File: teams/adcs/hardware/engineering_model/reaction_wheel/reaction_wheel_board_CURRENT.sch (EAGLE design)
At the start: 94 parts, among them U2 TPS732XX, U3 TPS732XX

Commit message: ADCS/RW: Clean up schematic
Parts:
- removed C26, C27: 2.2 μF, rcl:C-USC0805
- removed C32: 1 μF, rcl:C-USC0805
- removed C33: 22 μF, rcl:C-USC1206
- removed C34: 5.6 pF, rcl:C-USC0805
- removed C35: 10 μF, rcl:C-USC0805
- removed C36: 47 μF, rcl:C-USC1206
- removed D5: PMEG6010CEJ, DubSat1 Components:PMEG6010CEJ
- removed L2: WURTH_ELEKTRONIK_INDDD_744877001, DubSat1 Components:WURTH_ELEKTRONIK_INDDD_744877001
- removed R15: 1 kΩ, DubSat1 Components:RESISTOR0805
- removed R16: 330 kΩ, DubSat1 Components:RESISTOR0805
- removed R33: 120 kΩ, DubSat1 Components:RESISTOR0805
- removed U$6: LT8335, DubSat1 Components:LT8335
- C1, C11, C13, C15, C18, C20, C22, C3, C5: device rcl:C-USC1206 -> DubSat1 Components:CAPACITOR0805
- C12, C14, C19, C2, C21, C4: device rcl:C-USC0805 -> DubSat1 Components:CAPACITOR0805
- C16, C29: value 0.01 μF -> 0.01uF
- C17, C28, C30: value 1 μF -> 1uF
- C31: value 1μF -> 1uF
- C8: value 10 uF -> 10uF; device rcl:C-USC0805 -> DubSat1 Components:CAPACITOR0805
- R1, R17, R18, R19, R2, R24, R25, R26, R27, R3, R32, R8: value 3.3K -> 3.3k
- R10, R11, R9: value (none) -> 330
- R20, R21, R22, R28, R29, R30, R4, R5, R6: value 10K -> 10k
- R23, R31, R7: value (none) -> 273k
- U2, U3: value TPS732XX -> LT1761-X; device DubSat1 Components:TPS732XX -> DubSat1 Components:LT1761-X
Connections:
- removed net EN_UVLO: R15.2, U$6.EN/UVLO
- removed net FBX: C34.2, R16.1, R33.2, U$6.FBX
- removed net INT_VCC: C27.1, U$6.INT_VCC
- removed net SW: C32.1, L2.2A, U$6.SW@1, U$6.SW@2
- removed net VD: C32.2, D5.+, L2.1A
- removed net VM: C15.2, C22.2, C33.1, C34.1, C35.1, C36.1, C5.2, D5.-, R16.2, U$12.VM, U$15.VM, U$7.VM
- net GND: no longer C26.2, C27.2, C33.2, C35.2, C36.2, L2.1B, R33.1, U$6.GND
- net VBAT: now also C15.2, C22.2, C5.2, U$12.VM, U$15.VM, U$7.VM; no longer C26.1, L2.2B, R15.1, U$6.V_IN
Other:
- note added: "3v3 LDO"
- note added: "5v LDO"
- note added: "PC104 Header"
- note added: "X Motor Controller"
- note added: "X Motor Driver"
- note added: "Y Motor Controller"
- note added: "Y Motor Driver"
- note added: "Z Motor Controller"
- note added: "Z Motor Driver"
- moved on the sheet: C1, C11, C12, C13, C14, C15, C16, C17, C18, C19, C2, C20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

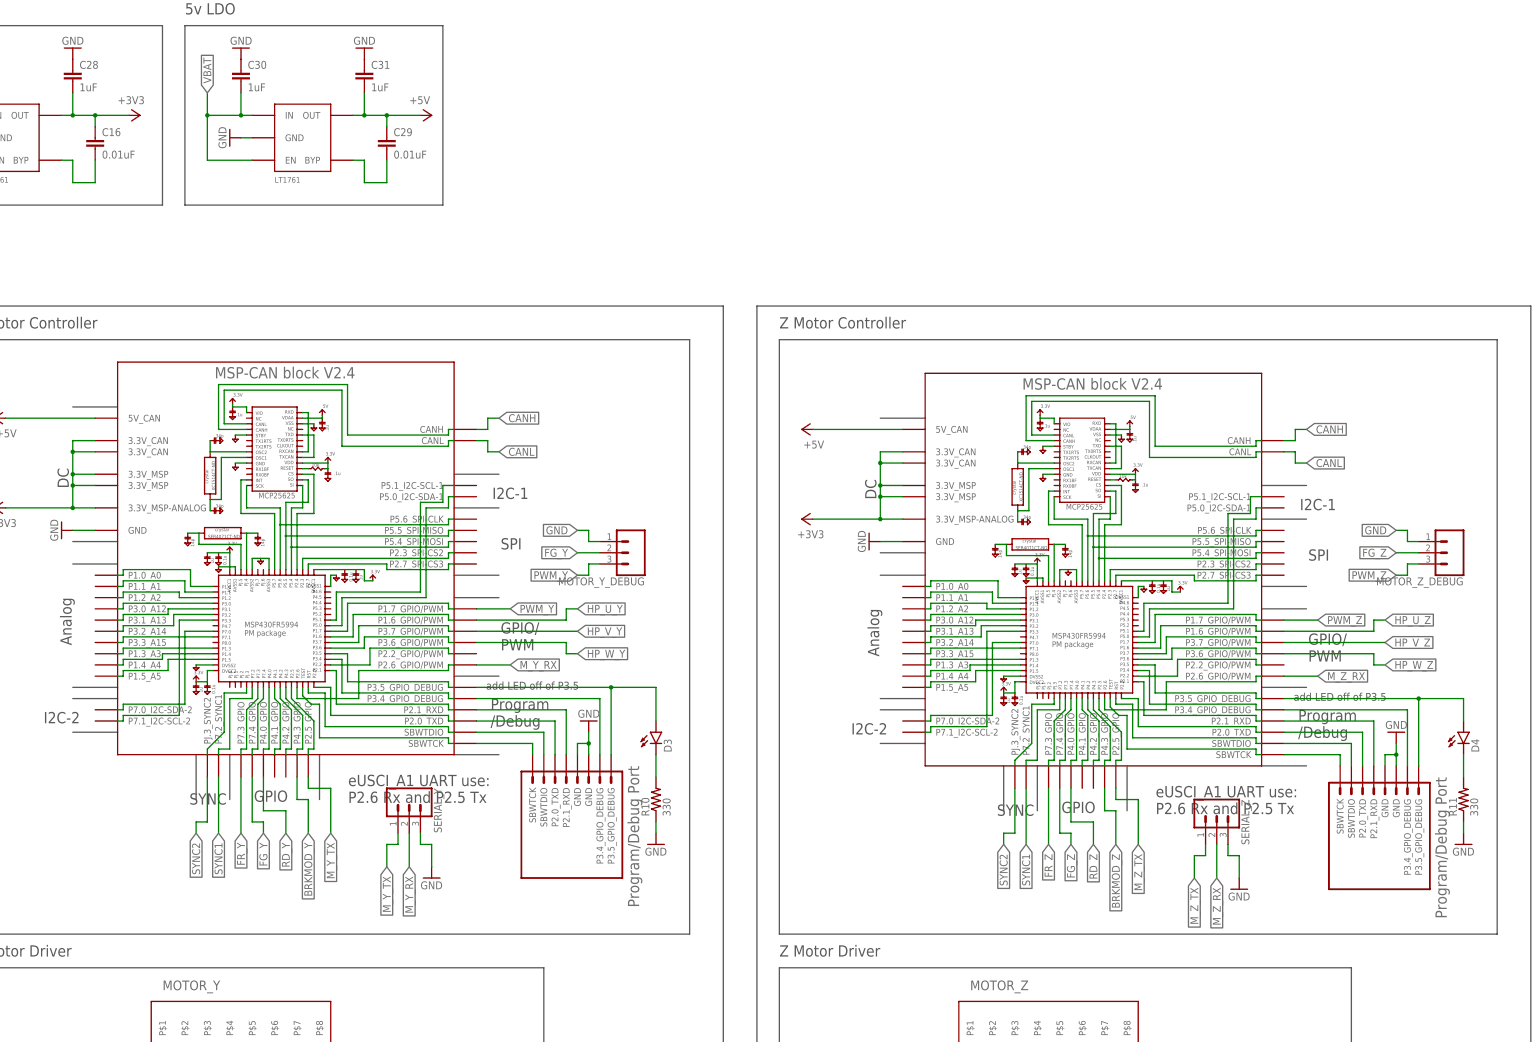
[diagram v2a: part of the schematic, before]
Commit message: ADCS/RW: Update LDO capacitor values
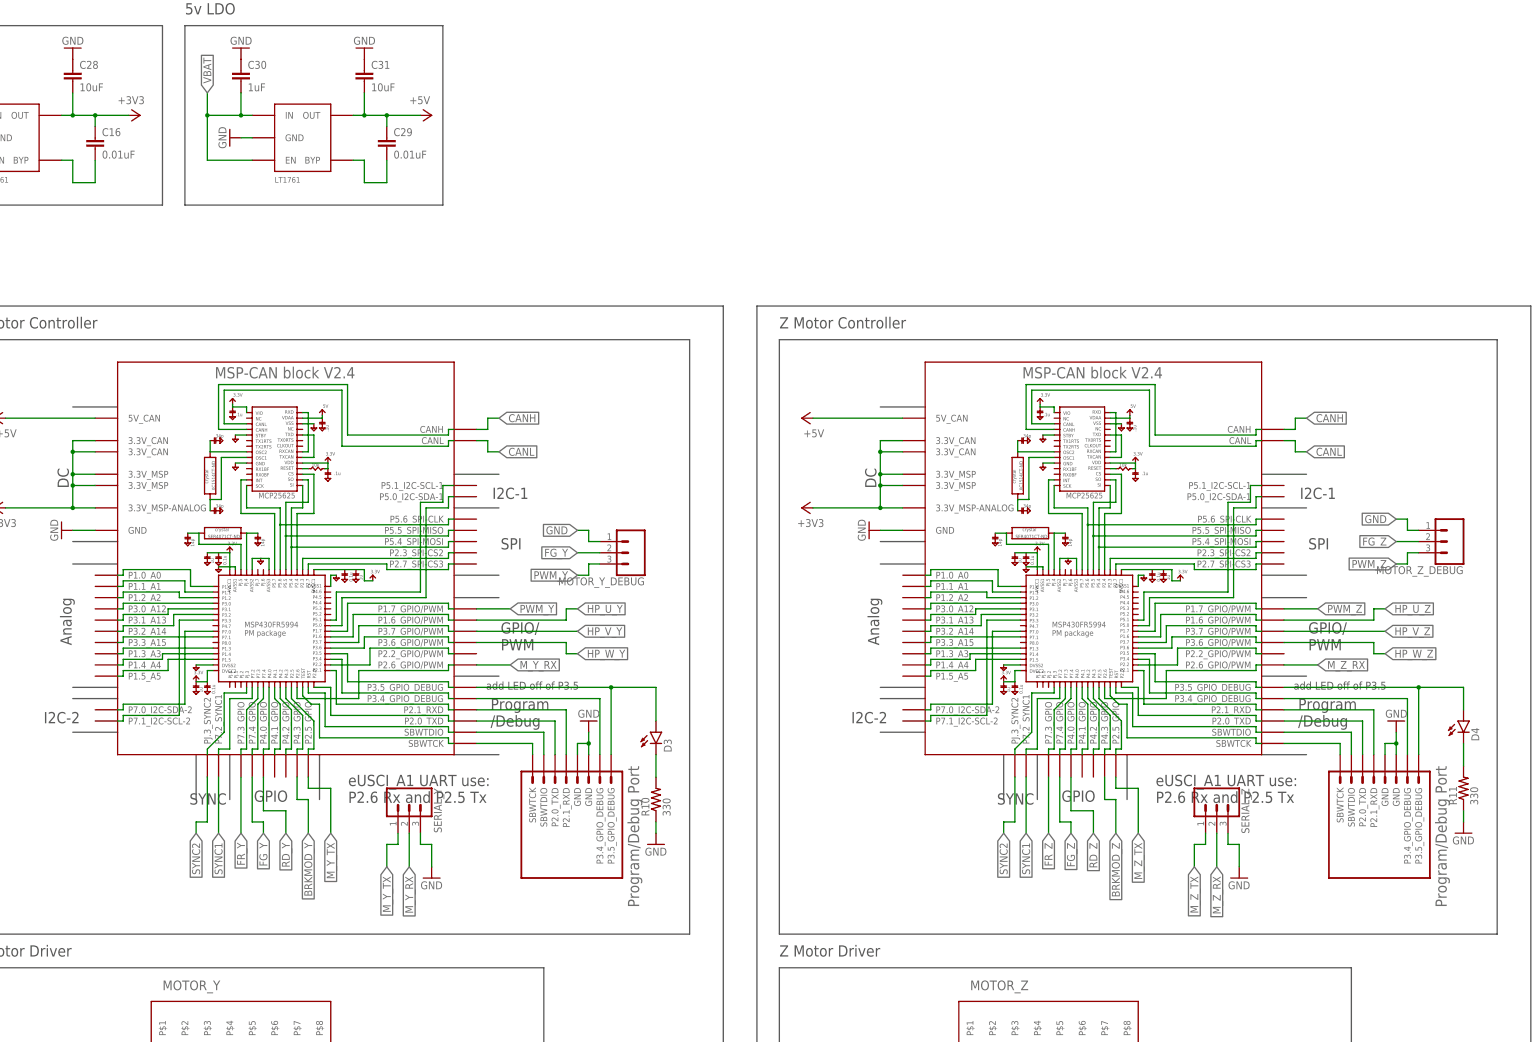
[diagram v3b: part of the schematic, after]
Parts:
- C28, C31: value 1uF -> 10uF
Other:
- moved on the sheet: D4, MOTOR_Z_DEBUG, R11, SERIAL_Z
